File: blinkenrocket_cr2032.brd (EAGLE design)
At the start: 96.3 x 47 mm, 22 parts, among them SW1 SWITCH-4POMRON-6-6-SWITCH, SW2 SWITCH-4POMRON-6-6-SWITCH, U2 EEPROM-I2CEIAJ

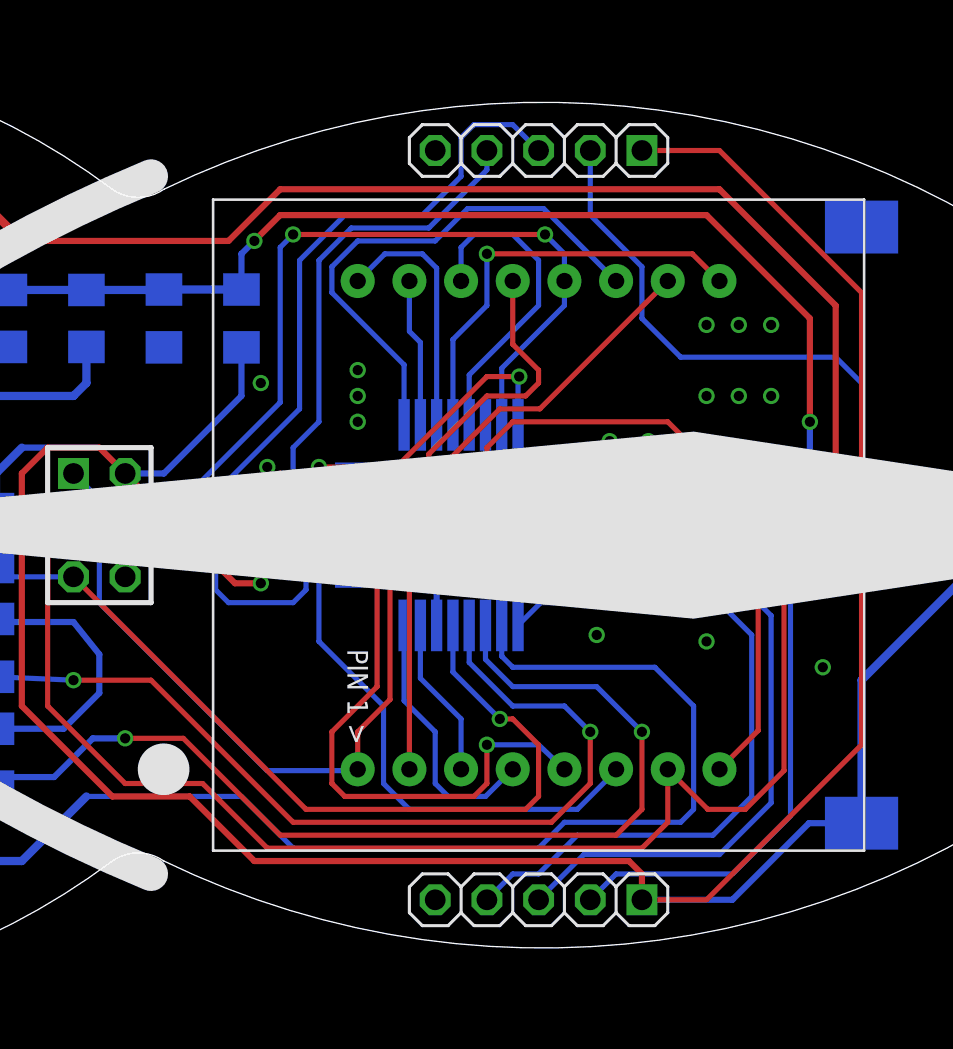
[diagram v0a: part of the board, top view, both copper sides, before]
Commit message: make the powersupply of the modem part switchable by the IC for powersaving reasons
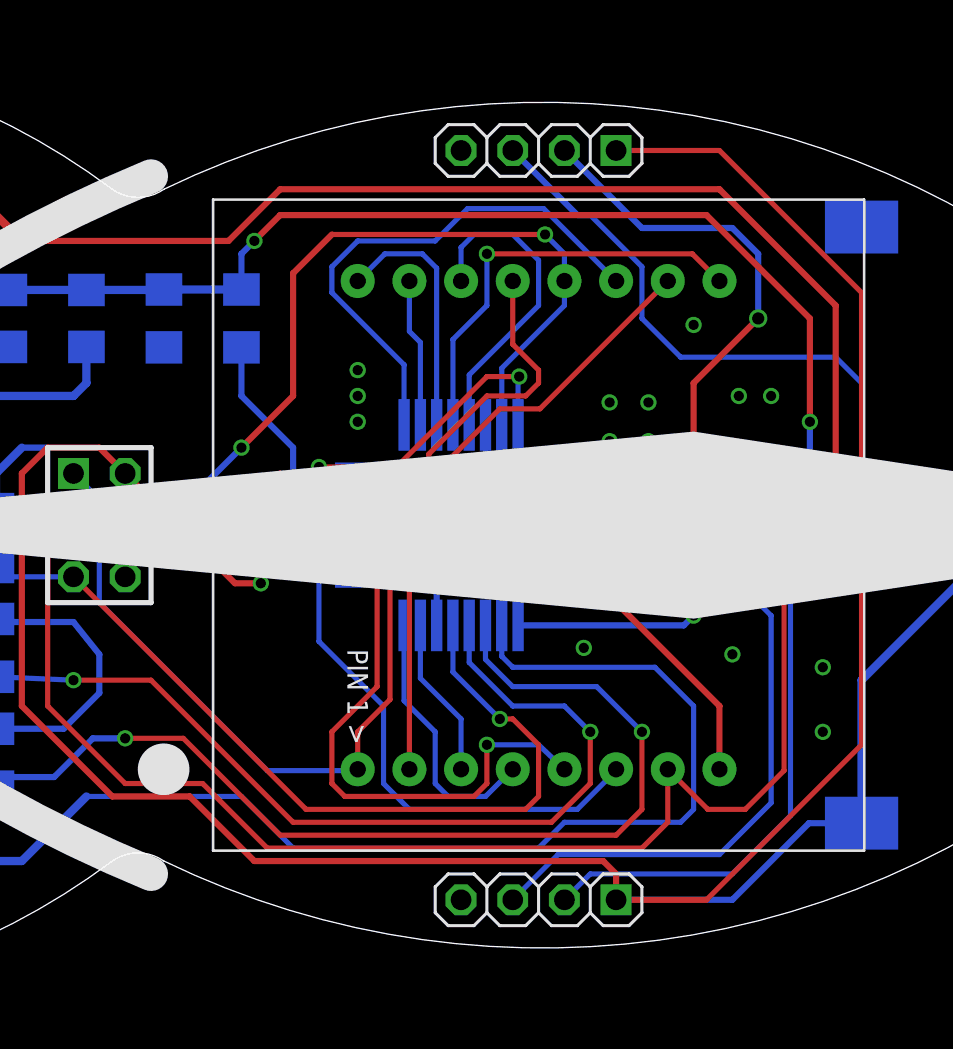
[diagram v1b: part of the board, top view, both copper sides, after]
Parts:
- JP3, JP4: device pinhead-2:1X05-S -> pinhead-2:1X04-S
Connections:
- removed net E5: JP4.3, U$2.3
- removed net E6: JP4.4, U$2.6
- new net TRIG1: U$2.3
- new net TRIG2: R1.2, U$2.6
- net E3: now also JP4.2; no longer JP3.4
- net E4: now also JP4.3; no longer JP4.2
- net GND: now also JP3.4, JP4.4; no longer JP3.5, JP4.5
- net VCC: no longer R1.2
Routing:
- net E5: track 43.1 -> 0.00 mm
- net E6: track 26.3 -> 0.00 mm
- net TRIG2: track 0.00 -> 11.1 mm
- net R3: track 32.8 -> 21.7 mm
- net VCC: track 203.7 -> 196.6 mm
- net E3: track 35.7 -> 39.6 mm, vias 0 -> 2
- net E4: track 43.5 -> 45.4 mm
- net E2: track 33.6 -> 34.9 mm
- net E1: track 34.0 -> 35.3 mm
- net R4/MOSI: track 42.0 -> 41.1 mm
- net GND: vias 26 -> 24
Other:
- board text removed: "E5"
- board text removed: "E6"
